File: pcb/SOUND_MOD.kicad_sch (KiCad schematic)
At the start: 16 parts, among them J6 Conn_01x06_Pin, U6 ME6211C33M5, U7 NS4168

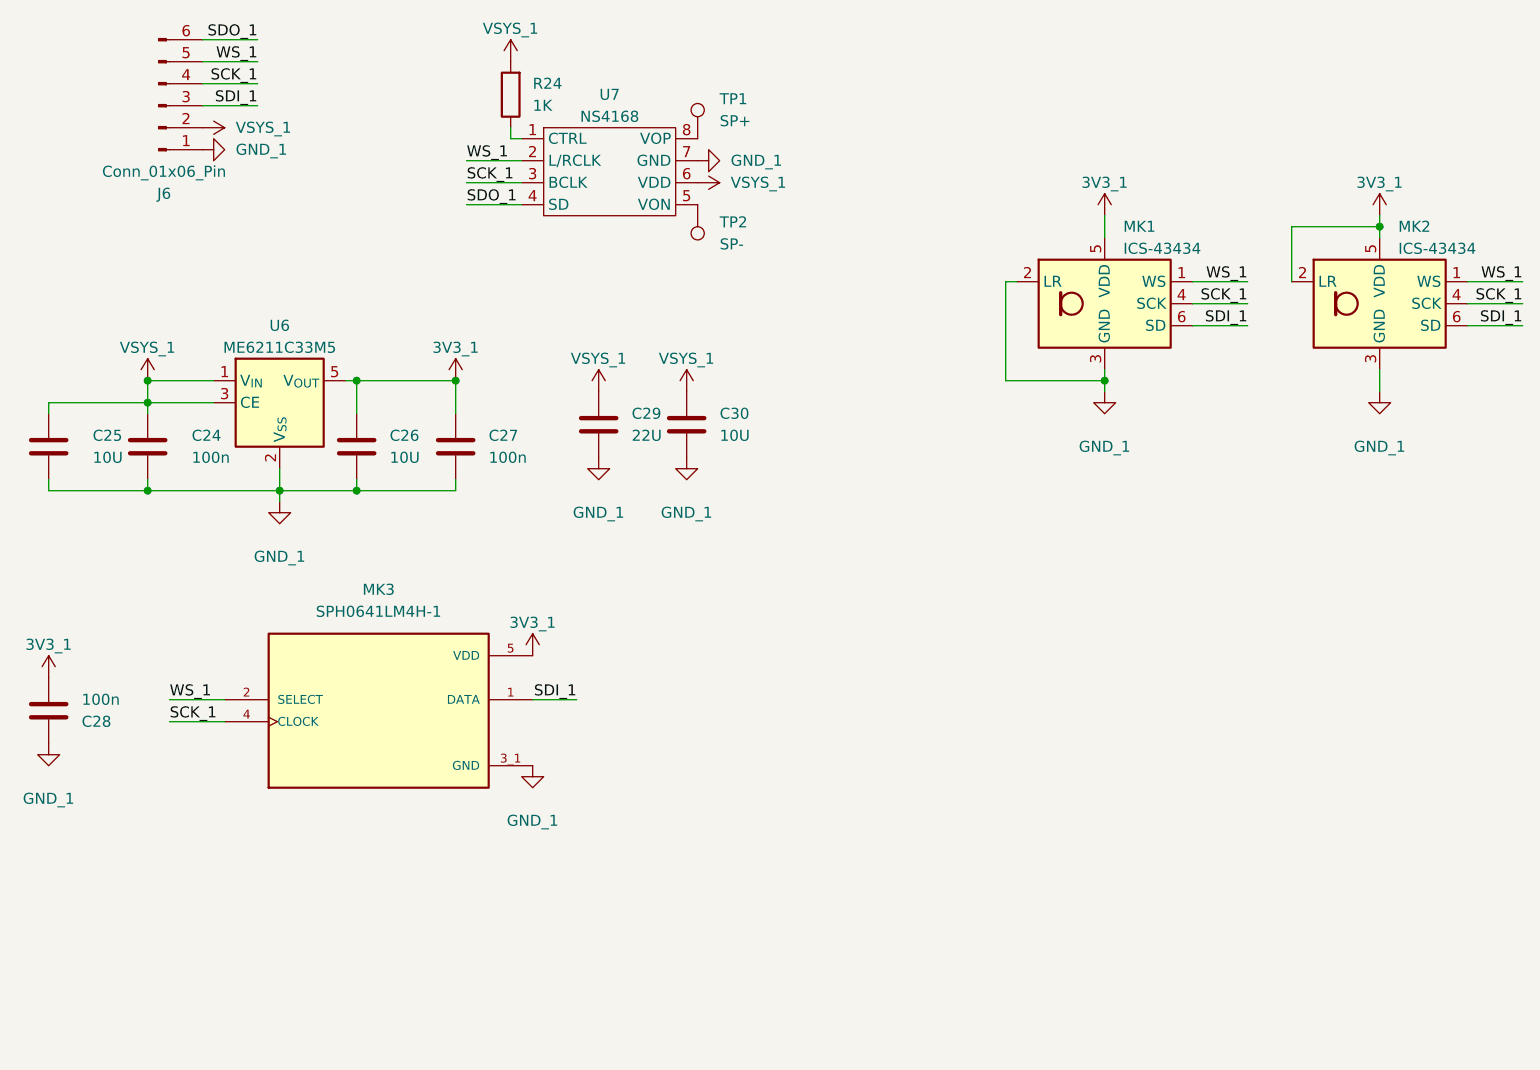
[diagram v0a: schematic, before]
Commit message: feat: improve pinout and remove sdcard and lora module, update design
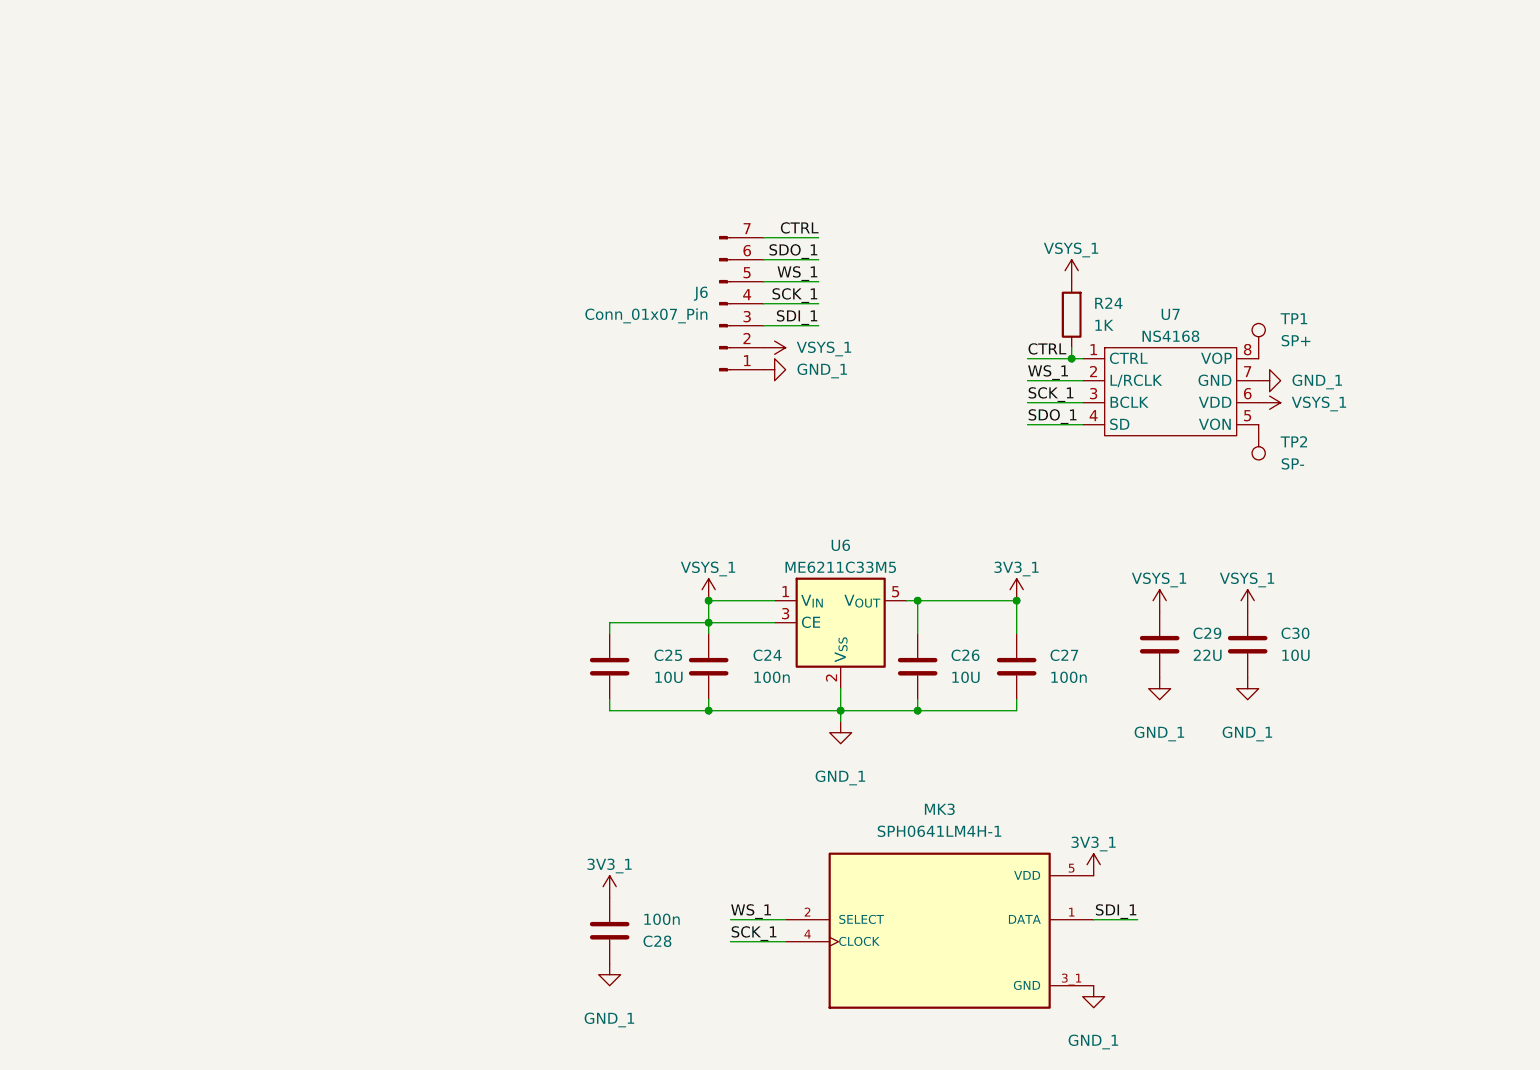
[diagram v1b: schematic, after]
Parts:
- removed J6: Conn_01x06_Pin, Connector_PinHeader_2.54mm:PinHeader_1x06_P2.54mm_Vertical, symbol Connector:Conn_01x06_Pin
- removed MK1, MK2: ICS-43434, Sensor_Audio:InvenSense_ICS-43434-6_3.5x2.65mm, symbol Sensor_Audio:ICS-43434
- added J6: Conn_01x07_Pin, Connector_PinHeader_2.54mm:PinHeader_1x07_P2.54mm_Vertical, symbol Connector:Conn_01x07_Pin
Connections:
- net GND: now also J6.1 (Pin_1)
- net SCK_1: now also J6.4 (Pin_4)
- net SDI_1: now also J6.3 (Pin_3)
- net SDO_1: now also J6.6 (Pin_6)
- net VSYS_1: now also J6.2 (Pin_2)
- net WS_1: now also J6.5 (Pin_5)
- net CTRL: now reaches R24.1, U7.1 (CTRL)
- net CTRL: now also J6.7 (Pin_7)
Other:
- moved on the sheet: C24, C25, C26, C27, C28, C29, C30, MK3, R24, TP1, TP2, U6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

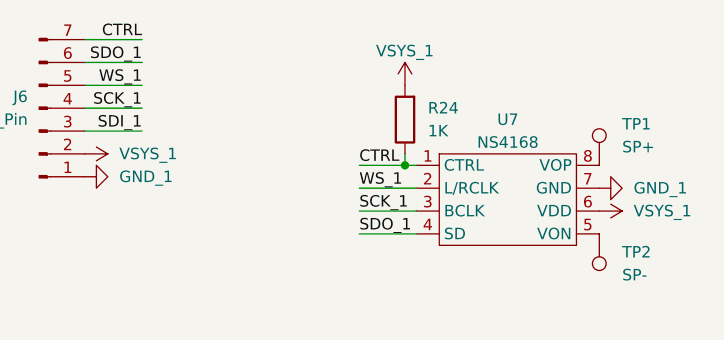
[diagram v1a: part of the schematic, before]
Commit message: fix sub ghz, epaper and audio module
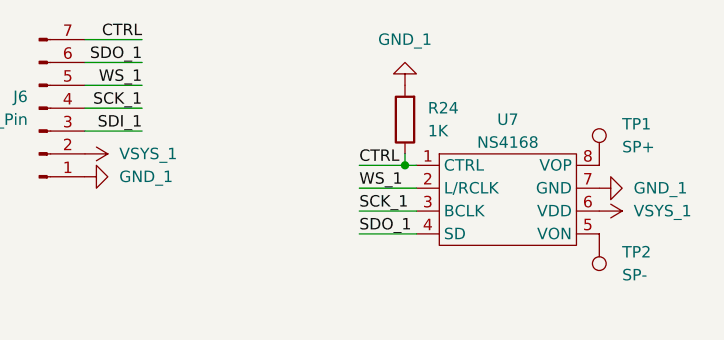
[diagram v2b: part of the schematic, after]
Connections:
- net GND: now also R24.2
- net VSYS_1: no longer R24.2
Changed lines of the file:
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@@
 	)
 	(symbol
-		(lib_id "power:VBUS")
-		(at 153.67 53.34 0)
+		(lib_id "power:GND")
+		(at 153.67 53.34 180)
 		(unit 1)
 		(exclude_from_sim no)
@@
 		(dnp no)
 		(fields_autoplaced yes)
-		(property "Reference" "#PWR084"
-			(at 153.67 57.15 0)
+		(property "Reference" "#PWR01"
+			(at 153.67 46.99 0)
 			(effects
 				(font
@@
 			)
 		)
-		(property "Value" "VSYS_1"
-			(at 153.67 49.53 0)
+		(property "Value" "GND_1"
+			(at 153.67 48.26 0)
 			(effects
 				(font
@@
 			)
 		)
-		(property "Description" "Power symbol creates a global label with name \"VBUS\""
+		(property "Description" "Power symbol creates a global label with name \"GND\" , ground"
 			(at 153.67 53.34 0)
 			(effects
@@
 		)
 		(instances
-			(project "lanyard"
+			(project "null-city-badge"
 				(path "/96a9ebd7-4f87-4060-87a7-f00d27473ddc/8c5168c8-f359-473b-9459-5b246b7098e5"
-					(reference "#PWR084")
+					(reference "#PWR01")
 					(unit 1)
 				)
